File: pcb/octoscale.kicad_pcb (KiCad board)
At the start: 2 copper layers, 60 x 96.5 mm, 109 parts, among them J1 USB_C_Receptacle_USB2.0 TYPE-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, J2 Conn_01x04_Male, J3 Conn_01x02_Female, J4 JST-SH, stemma, J5 JST-SH, stemma, J6 JST-SH, stemma, Q1 AO3415_C181094, Q2 MMBT44032T, Q3 S8050, SW1 SW_Push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

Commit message: Move load cell
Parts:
- removed kibuzzard-629F2581: G***, kibuzzard-629F2581
- added kibuzzard-62A1FF38: G***, kibuzzard-62A1FF38, B.Cu at (194.8, 114.8)
- moved kibuzzard-629CDB8B 70.9 mm to (181.1, 52.2), turned to 0 degrees
- moved C21 3.69 mm to (194.3, 63.9)
- moved C26 3.59 mm to (196.3, 76.5)
- moved R19 2.76 mm to (187.3, 112.9)
- moved J5 2.15 mm to (190.4, 70.8)
- moved R17 2.06 mm to (186.4, 128.2), turned to -90 degrees
- moved kibuzzard-629CD693 1.92 mm to (186.9, 102.5)
- moved J6 1.90 mm to (188.9, 64.0)
- moved R18 1.81 mm to (188.7, 116.1), turned to 180 degrees
- moved kibuzzard-629CD677 1.60 mm to (197.6, 102.5)
- moved SW2 1.58 mm to (190.1, 102.7)
- moved SW1 1.40 mm to (194.1, 102.7)
- moved kibuzzard-629E3B4E 1.30 mm to (195.4, 66.7)
- moved REF** 1.30 mm to (177.8, 95.0)
- moved LS1 1.05 mm to (190.3, 78.8)
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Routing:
- net +3V3: track 219.3 -> 224.0 mm
- net +BATT: track 297.6 -> 300.7 mm
- net SCL: track 85.4 -> 87.8 mm
- net EXP_1_B: track 50.7 -> 52.8 mm
- net EXP_1_A: track 50.4 -> 52.6 mm
- net EXP_2_B: track 43.9 -> 45.8 mm
- net EXP_2_A: track 45.0 -> 46.9 mm
- net BOOT: track 36.9 -> 38.5 mm
- net Net-(DS1-Pad26): track 13.3 -> 14.9 mm
- net Net-(C17-Pad2): track 12.6 -> 13.6 mm
- net Net-(C18-Pad2): track 12.1 -> 13.1 mm
- net RESET: track 53.7 -> 54.4 mm

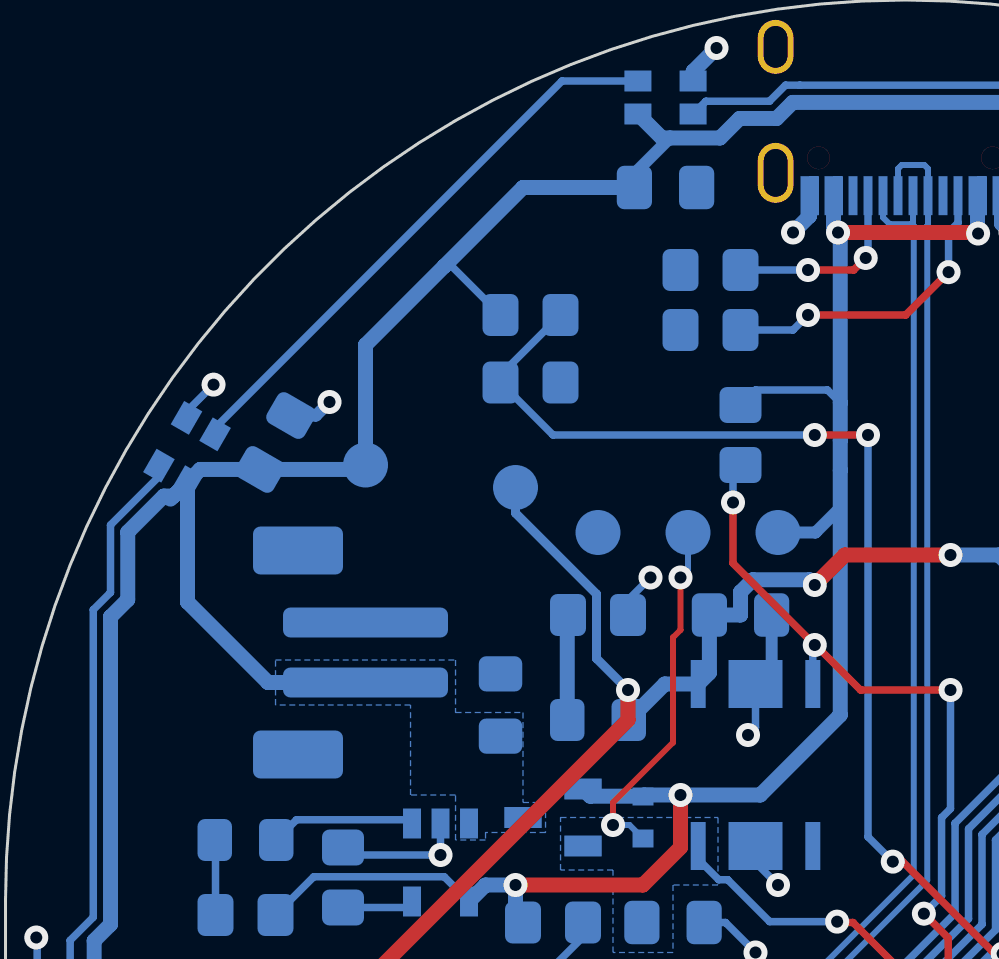
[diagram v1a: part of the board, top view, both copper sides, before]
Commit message: Move battery connector
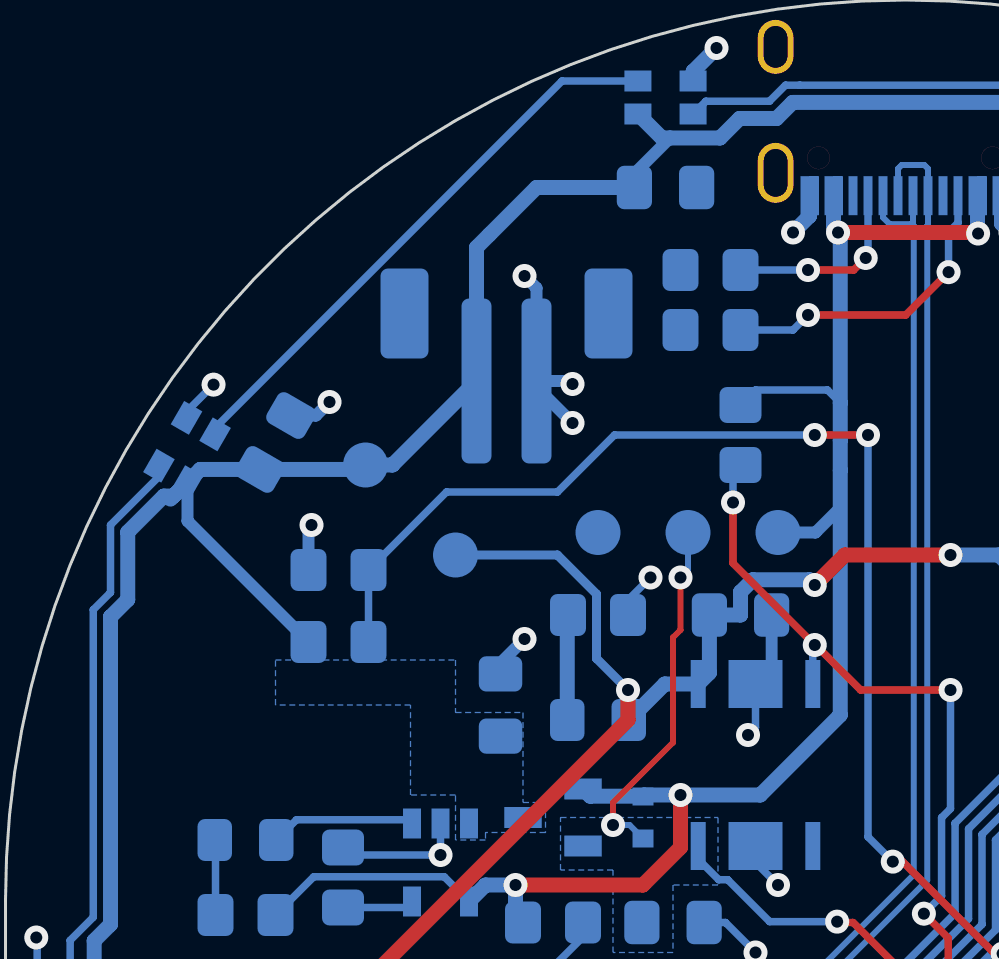
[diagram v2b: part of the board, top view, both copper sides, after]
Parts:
- moved R16 12.6 mm to (151.1, 66.4)
- moved J3 10.9 mm to (156.7, 57.2), turned to 180 degrees
- moved R20 8.95 mm to (151.1, 64.0), turned to 180 degrees
- moved TP12 3.01 mm to (155.0, 63.5)
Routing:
- net GND: track 120.8 -> 130.6 mm, vias 39 -> 44
- net +BATT: track 300.7 -> 294.4 mm
- net BATT_SENSE: track 56.5 -> 61.3 mm
- net +3V3: track 224.0 -> 224.9 mm

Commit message: first draft of case
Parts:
- J3: value Conn_01x02_Female -> JST PH Vertical C64658
- J5, J6: value JST-SH, stemma -> JST-SH
- moved TP12 9.98 mm to (147.1, 69.6)
- moved TP6 7.97 mm to (159.5, 63.2)
- moved TP10 7.59 mm to (152.3, 61.3)
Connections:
- DS1 pad 10: GND -> unconnected-(DS1-Pad10)
- J1 pad S1: (no net) -> GND
- J3 pad 1: GND -> +BATT
- J3 pad 2: +BATT -> GND
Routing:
- net +BATT: track 294.4 -> 310.3 mm
- net GND: track 130.6 -> 134.6 mm, vias 44 -> 45
- net BATT_SENSE: track 61.3 -> 58.5 mm, vias 6 -> 8
- net EXP_1_B: track 52.8 -> 55.2 mm
- net EXP_1_A: track 52.6 -> 54.8 mm
- net EXP_2_A: track 46.9 -> 49.1 mm
- net LDO_EN: track 51.7 -> 50.6 mm
- net EXP_2_B: track 45.8 -> 46.7 mm
- net +3V3: track 224.9 -> 225.2 mm, vias 10 -> 9
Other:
- board text added: "+"
- board text added: "-"

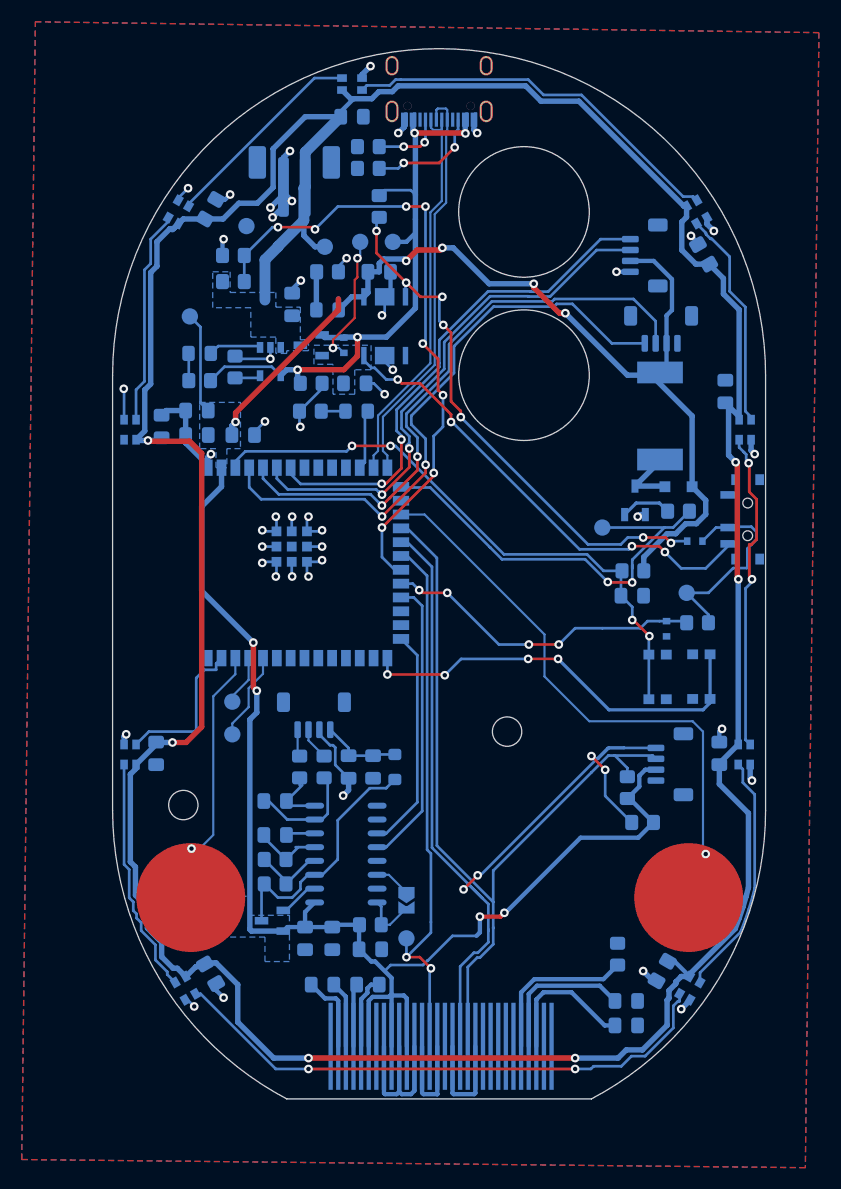
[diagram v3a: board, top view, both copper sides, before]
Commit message: Change battery connector and load cell
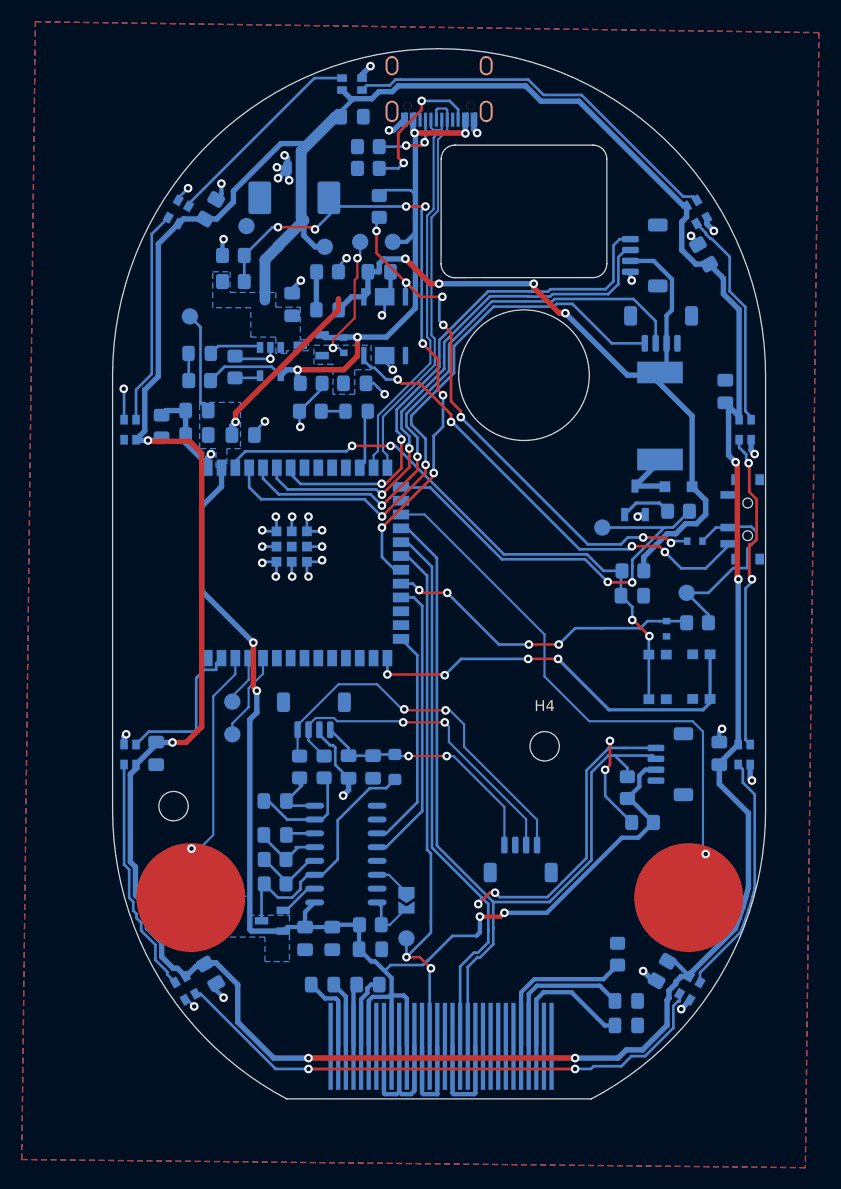
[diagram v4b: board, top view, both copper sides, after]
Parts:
- added J7: Conn_01x04_Male, Connector_JST:JST_SH_BM04B-SRSS-TB_1x04-1MP_P1.00mm_Vertical, B.Cu at (177.5, 119.5)
- J3: value JST PH Vertical C64658 -> Molex picoblade vertical C122410; footprint Connector_JST:JST_PH_B2B-PH-SM4-TB_1x02-1MP_P2.00mm_Vertical -> Connector_Molex:Molex_PicoBlade_53398-0271_1x02-1MP_P1.25mm_Vertical
- moved H4 3.70 mm to (179.7, 109.1)
- moved kibuzzard-629E3B7C 1.00 mm to (190.0, 56.8)
- moved H2 0.91 mm to (145.6, 114.6)
- moved kibuzzard-629CDB8B 0.41 mm to (181.2, 51.8), turned to 180 degrees
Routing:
- net /A+: track 2.50 -> 35.2 mm, vias 0 -> 2
- net /A-: track 3.02 -> 30.8 mm, vias 0 -> 2
- net /ADD: track 7.38 -> 22.9 mm, vias 0 -> 2
- net +BATT: track 310.3 -> 304.4 mm
- net GND: track 134.6 -> 128.7 mm
- net /CC2: track 10.4 -> 13.9 mm
- net SDA: track 77.4 -> 80.4 mm
- net EXP_2_B: track 46.7 -> 48.7 mm
- net EXP_2_A: track 49.1 -> 50.5 mm
- net +3V3: track 225.2 -> 224.2 mm
- net SCL: track 87.8 -> 88.6 mm
- net D-: track 37.3 -> 36.7 mm
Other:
- board text added: "According to all known laws of aviation, there is no way a bee should be able to fly. Its wings are too small to get its fat little body off the ground. The bee, of course, flies anyway because bees don't care what humans think is impossible. Yellow, black. Yellow, black. Yellow, black. Yellow, black. Ooh, black and yellow! Let's shake it up a little. Barry! Breakfast is ready! Coming! Hang on a 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"
- board text added: "Red Black White Grn|Blue"
- board text added: "gp 4 gp 5 3.3v gnd"
- board text added: "gp 7 gp 6 3.3v gnd"
- board text removed: "According to all known laws of aviation, there is no way a bee should be able to fly. Its wings are too small to get its fat little body off the ground. The bee, of course, flies anyway because bees don't carewhat humans think is impossible. Yellow, black. Yellow, black. Yellow, black. Yellow, black. Ooh, black and yellow! Let's shake it up a little. Barry! Breakfast is ready! Coming! Hang on a s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"
- board text removed: "gpio 4 gpio 5 3.3v gnd"
- board text removed: "gpio 7 gpio 6 3.3v gnd"

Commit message: Change oled to ssd1306 and fix hx711 agnd
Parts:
- added C28: 10uF, Capacitor_SMD:C_0805_2012Metric_Pad1.18x1.45mm_HandSolder, B.Cu at (169.2, 130.7)
- added C29: 1uF, Capacitor_SMD:C_0805_2012Metric_Pad1.18x1.45mm_HandSolder, B.Cu at (169.2, 128.5)
- C15, C16: value 1uF -> 2.2uF
- C17: value 4.7uF -> 10uF
- C18: value 2.2uF -> 10uF
- R17: value 400k -> 300k
- moved TP8 0.55 mm to (167.0, 126.2)
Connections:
- C7 pad 1: Net-(C7-Pad1) -> GND
- DS1 pad 10: unconnected-(DS1-Pad10) -> GND
- DS1 pad 13: GND -> +3V3
- DS1 pad 16: GND -> unconnected-(DS1-Pad16)
- DS1 pad 17: GND -> unconnected-(DS1-Pad17)
- DS1 pad 20: GND -> SDA
- DS1 pad 21: GND -> unconnected-(DS1-Pad21)
- DS1 pad 22: GND -> unconnected-(DS1-Pad22)
- DS1 pad 23: GND -> unconnected-(DS1-Pad23)
- DS1 pad 24: GND -> unconnected-(DS1-Pad24)
- DS1 pad 25: GND -> unconnected-(DS1-Pad25)
- R9 pad 2: Net-(C7-Pad1) -> GND
- U4 pad 5: Net-(C7-Pad1) -> GND
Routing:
- net +3V3: track 224.2 -> 245.0 mm
- net unconnected-(DS1-Pad17): track 0.00 -> 10.8 mm
- net Net-(C7-Pad1): track 6.44 -> 0.00 mm
- net OLED_RESET: track 50.9 -> 51.4 mm
- net GND: track 128.7 -> 129.1 mm, vias 45 -> 50

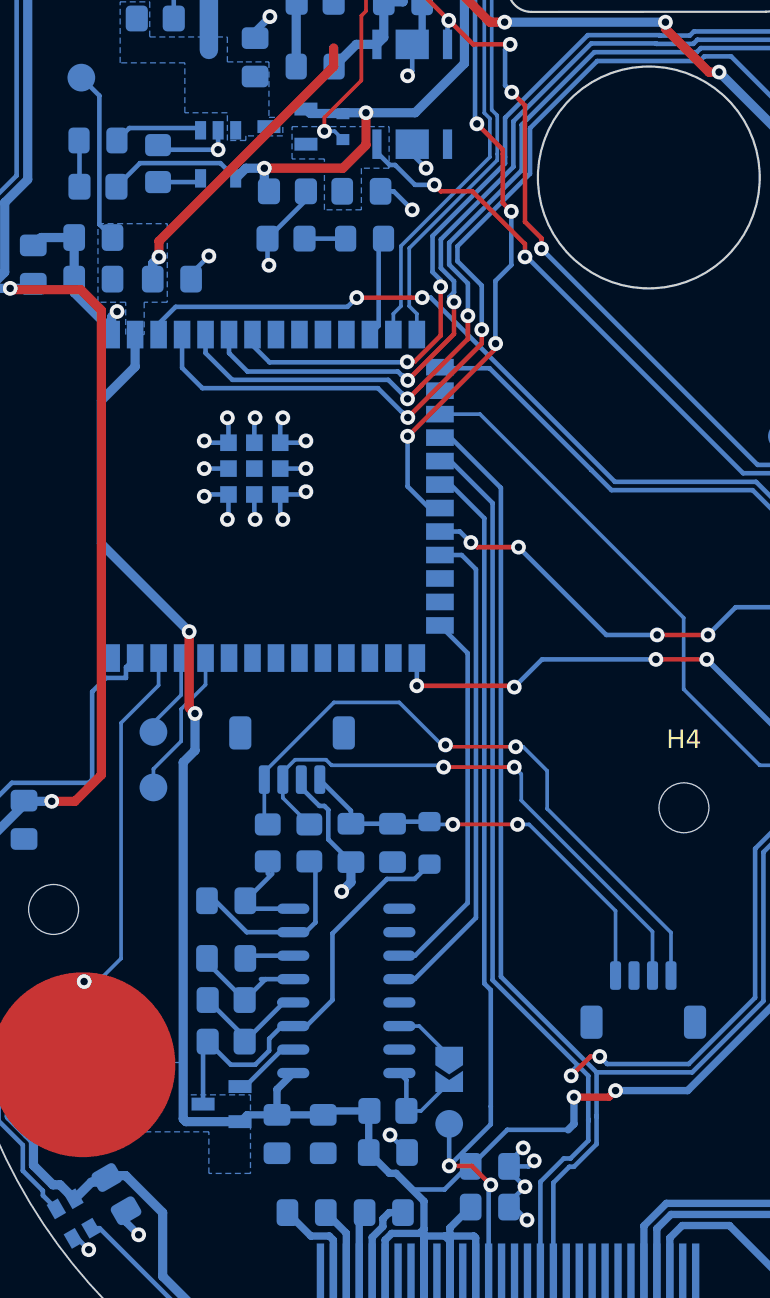
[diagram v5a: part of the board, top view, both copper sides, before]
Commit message: Move touch 2 pins
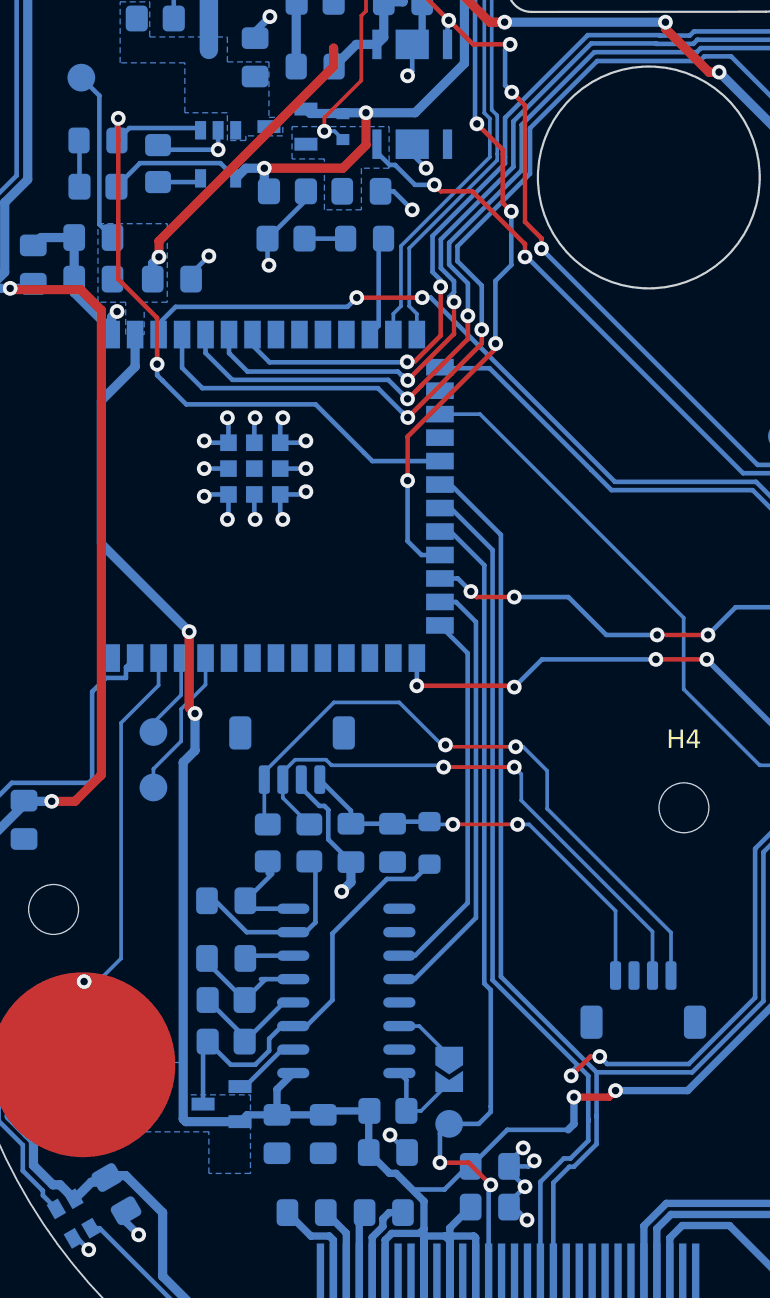
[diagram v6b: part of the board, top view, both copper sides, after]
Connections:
- D5 pad 1: Net-(D5-Pad1) -> CHRG
- U1 pad 1: Net-(D5-Pad1) -> CHRG
- U5 pad 18: SDA -> unconnected-(U5-Pad18)
- U5 pad 19: SCL -> CHRG
- U5 pad 20: OLED_RESET -> SDA
- U5 pad 21: BATT_SENSE -> SCL
- U5 pad 22: POWER_SWITCH_SENSE -> OLED_RESET
- U5 pad 23: SCALE_DATA -> BATT_SENSE
- U5 pad 24: unconnected-(U5-Pad24) -> POWER_SWITCH_SENSE
- U5 pad 25: unconnected-(U5-Pad25) -> SCALE_DATA
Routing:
- net CHRG: track 0.00 -> 38.1 mm, vias 0 -> 2
- net unconnected-(DS1-Pad17): track 10.8 -> 0.00 mm
- net SDA: track 80.4 -> 88.7 mm
- net Net-(D5-Pad1): track 4.86 -> 0.00 mm
- net OLED_RESET: track 51.4 -> 48.2 mm
- net BATT_SENSE: track 58.6 -> 61.3 mm
- net SCALE_DATA: track 26.6 -> 23.9 mm
- net SCL: track 88.6 -> 86.6 mm
- net POWER_SWITCH_SENSE: track 29.5 -> 28.5 mm
